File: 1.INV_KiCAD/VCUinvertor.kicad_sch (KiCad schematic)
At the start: 159 parts, among them J10 FAN2, J11 PUMP1, J12 PUMP2, J7 PowerSupply, J8 FAN1, J9 BRAKE LIGHT, K1 IM06DGR, Q1 2N7002, Q10 2N7002, Q11 2N7002, Q12 2N7002, Q13 BC848C, Q14 2N7002, Q15 IRLZ44N, Q16 IRLZ44N, Q17 IRLZ44N, Q18 2N7002, Q19 IRLZ44N, Q2 2N7002, Q3 2N7002, Q4 2N7002, Q5 2N7002, Q6 2N7002, Q7 2N7002, Q8 2N7002, Q9 2N7002, U1 TJA1448ATK, U2 REF3433T, U3 TLV76150DCY

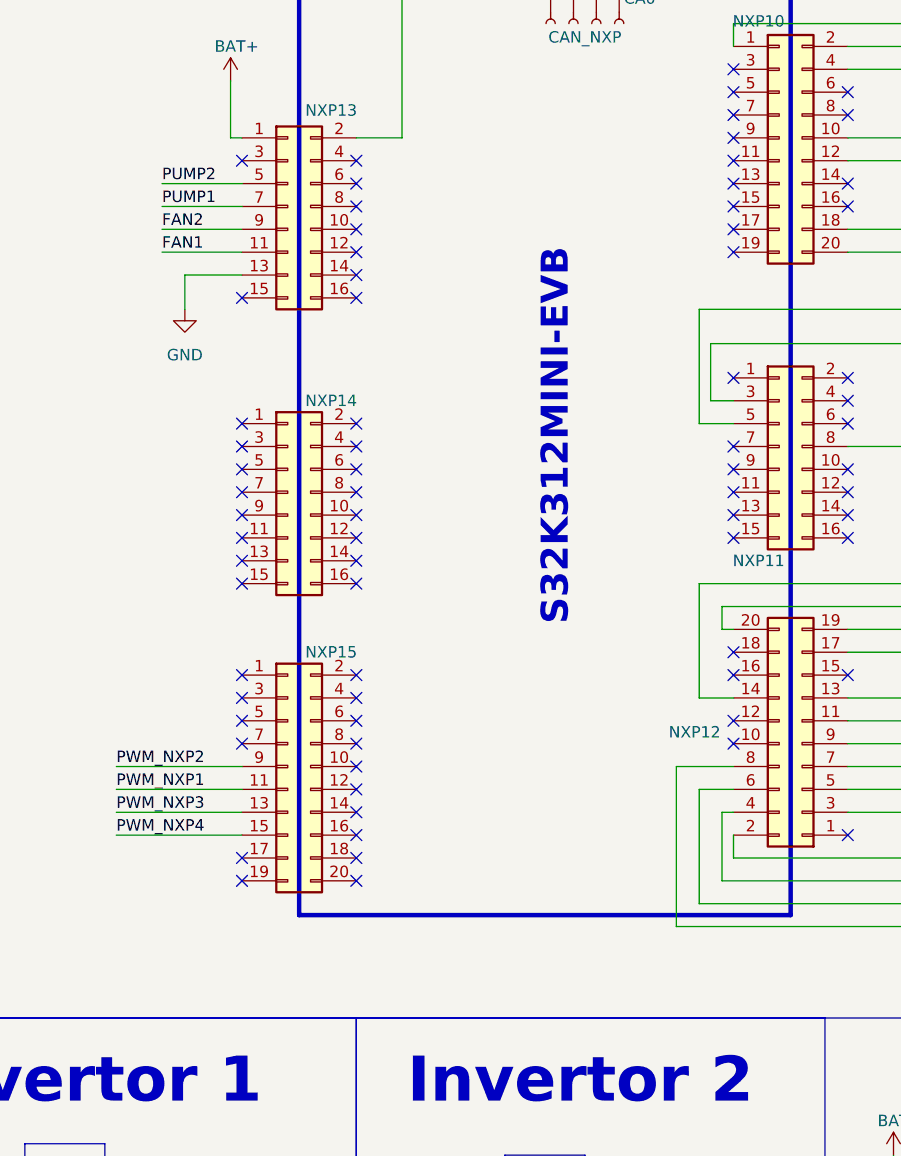
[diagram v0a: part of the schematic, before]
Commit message: FAN&PUMP pin change
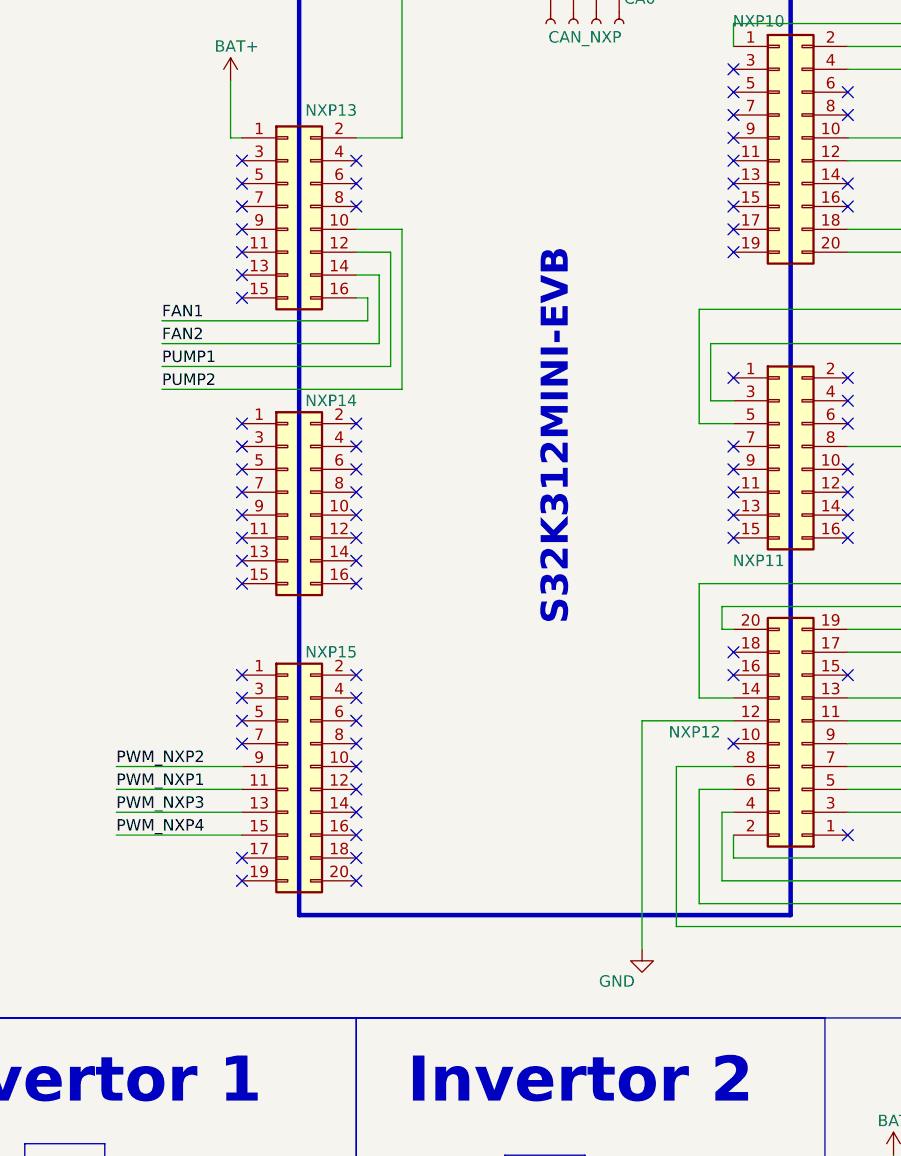
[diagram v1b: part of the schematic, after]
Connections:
- net FAN1: now also NXP13.16 (Pin_16); no longer NXP13.11 (Pin_11)
- net FAN2: now also NXP13.14 (Pin_14); no longer NXP13.9 (Pin_9)
- net GND: now also NXP12.12 (Pin_12); no longer NXP13.13 (Pin_13)
- net PUMP1: now also NXP13.12 (Pin_12); no longer NXP13.7 (Pin_7)
- net PUMP2: now also NXP13.10 (Pin_10); no longer NXP13.5 (Pin_5)

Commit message: Pin - GND assignment
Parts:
- R23: value 10k -> 47k
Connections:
- net FAN1: now also NXP13.14 (Pin_14); no longer NXP13.16 (Pin_16)
- net FAN2: now also NXP13.12 (Pin_12); no longer NXP13.14 (Pin_14)
- net GND: now also NXP13.13 (Pin_13)
- net PUMP1: now also NXP13.9 (Pin_9); no longer NXP13.12 (Pin_12)
- no-connect marks 81 -> 80
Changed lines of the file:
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@@
 	)
 	(no_connect
-		(at 54.61 63.5)
-	)
-	(no_connect
 		(at 109.22 60.96)
 	)
@@
 	)
 	(no_connect
-		(at 54.61 66.04)
-	)
-	(no_connect
 		(at 54.61 85.09)
 	)
@@
 	)
 	(no_connect
+		(at 54.61 63.5)
+	)
+	(no_connect
 		(at 121.92 90.17)
 	)
@@
 	)
 	(no_connect
-		(at 54.61 60.96)
-	)
-	(no_connect
 		(at 31.75 185.42)
 	)
@@
 	)
 	(no_connect
+		(at 67.31 68.58)
+	)
+	(no_connect
 		(at 109.22 92.71)
 	)
@@
 	(wire
 		(pts
+			(xy 40.64 66.04) (xy 54.61 66.04)
+		)
+		(stroke
+			(width 0)
+			(type default)
+		)
+	)
+	(wire
+		(pts
 			(xy 121.92 125.73) (xy 143.51 125.73)
 		)
@@
 	(wire
 		(pts
-			(xy 68.58 68.58) (xy 68.58 71.12)
-		)
-		(stroke
-			(width 0)
-			(type default)
-		)
-	)
-	(wire
-		(pts
 			(xy 138.43 251.46) (xy 138.43 254)
 		)
@@
 	(wire
 		(pts
-			(xy 67.31 66.04) (xy 69.85 66.04)
+			(xy 40.64 66.04) (xy 40.64 71.12)
 		)
 		(stroke
@@
 	(wire
 		(pts
-			(xy 16.51 166.37) (xy 27.94 166.37)
+			(xy 67.31 66.04) (xy 69.85 66.04)
 		)
 		(stroke
@@
 	(wire
 		(pts
-			(xy 67.31 60.96) (xy 72.39 60.96)
+			(xy 16.51 166.37) (xy 27.94 166.37)
 		)
 		(stroke
@@
 	(wire
 		(pts
-			(xy 67.31 68.58) (xy 68.58 68.58)
+			(xy 67.31 60.96) (xy 72.39 60.96)
 		)
 		(stroke
@@
 	(wire
 		(pts
+			(xy 45.72 60.96) (xy 54.61 60.96)
+		)
+		(stroke
+			(width 0)
+			(type default)
+		)
+	)
+	(wire
+		(pts
 			(xy 233.68 223.52) (xy 234.95 223.52)
 		)
@@
 	(wire
 		(pts
-			(xy 45.72 71.12) (xy 68.58 71.12)
-		)
-		(stroke
-			(width 0)
-			(type default)
-		)
-	)
-	(wire
-		(pts
 			(xy 138.43 270.51) (xy 143.51 270.51)
 		)
@@
 		)
 	)
-	(label "FAN1"
-		(at 45.72 71.12 0)
-		(effects
-			(font
-				(size 1.27 1.27)
-			)
-			(justify left bottom)
-		)
-	)
 	(label "12V_INV"
 		(at 218.44 147.32 0)
@@
 		)
 	)
+	(label "PUMP1"
+		(at 45.72 60.96 0)
+		(effects
+			(font
+				(size 1.27 1.27)
+			)
+			(justify left bottom)
+		)
+	)
 	(label "Brk_AN1"
 		(at 393.7 54.61 180)
@@
 		)
 	)
+	(label "FAN2"
+		(at 45.72 76.2 0)
+		(effects
+			(font
+				(size 1.27 1.27)
+			)
+			(justify left bottom)
+		)
+	)
 	(label "5V"
 		(at 349.25 134.62 0)
@@
 		)
 	)
+	(label "FAN1"
+		(at 45.72 73.66 0)
+		(effects
+			(font
+				(size 1.27 1.27)
+			)
+			(justify left bottom)
+		)
+	)
 	(label "ACC1"
 		(at 16.51 189.23 0)
@@
 		)
 	)
-	(label "PUMP1"
-		(at 45.72 76.2 0)
-		(effects
-			(font
-				(size 1.27 1.27)
-			)
-			(justify left bottom)
-		)
-	)
 	(label "FWD2"
 		(at 71.12 201.93 0)
@@
 		)
 	)
-	(label "FAN2"
-		(at 45.72 73.66 0)
-		(effects
-			(font
-				(size 1.27 1.27)
-			)
-			(justify left bottom)
-		)
-	)
 	(label "ECO2"
 		(at 246.38 175.26 180)
@@
 	)
 	(symbol
+		(lib_id "power:GND")
+		(at 40.64 71.12 0)
+		(unit 1)
+		(body_style 1)
+		(exclude_from_sim no)
+		(in_bom yes)
+		(on_board yes)
+		(in_pos_files yes)
+		(dnp no)
+		(property "Reference" "#PWR073"
+			(at 40.64 77.47 0)
+			(hide yes)
+			(show_name no)
+			(do_not_autoplace no)
+			(effects
+				(font
+					(size 1.27 1.27)
+				)
+			)
+		)
+		(property "Value" "GND"
+			(at 37.846 74.676 0)
+			(show_name no)
+			(do_not_autoplace no)
+			(effects
+				(font
+					(size 1.27 1.27)
+				)
+			)
+		)
+		(property "Footprint" ""
+			(at 40.64 71.12 0)
+			(hide yes)
+			(show_name no)
+			(do_not_autoplace no)
+			(effects
+				(font
+					(size 1.27 1.27)
+				)
+			)
+		)
+		(property "Datasheet" ""
+			(at 40.64 71.12 0)
+			(hide yes)
+			(show_name no)
+			(do_not_autoplace no)
+			(effects
+				(font
+					(size 1.27 1.27)
+				)
+			)
+		)
+		(property "Description" "Power symbol creates a global label with name \"GND\" , ground"
+			(at 40.64 71.12 0)
+			(hide yes)
+			(show_name no)
+			(do_not_autoplace no)
+			(effects
+				(font
+					(size 1.27 1.27)
+				)
+			)
+		)
+		(pin "1"
+		)
+		(instances
+			(project "VCUinvertor"
+				(path "/2b4b6758-f217-4dbc-8f9c-9ada5d4e488c"
+					(reference "#PWR073")
+					(unit 1)
+				)
+			)
+		)
+	)
+	(symbol
 		(lib_id "power:+12V")
 		(at 137.16 204.47 0)
@@
 			)
 		)
-		(property "Value" "10k"
+		(property "Value" "47k"
 			(at 346.202 235.712 90)
 			(show_name no)

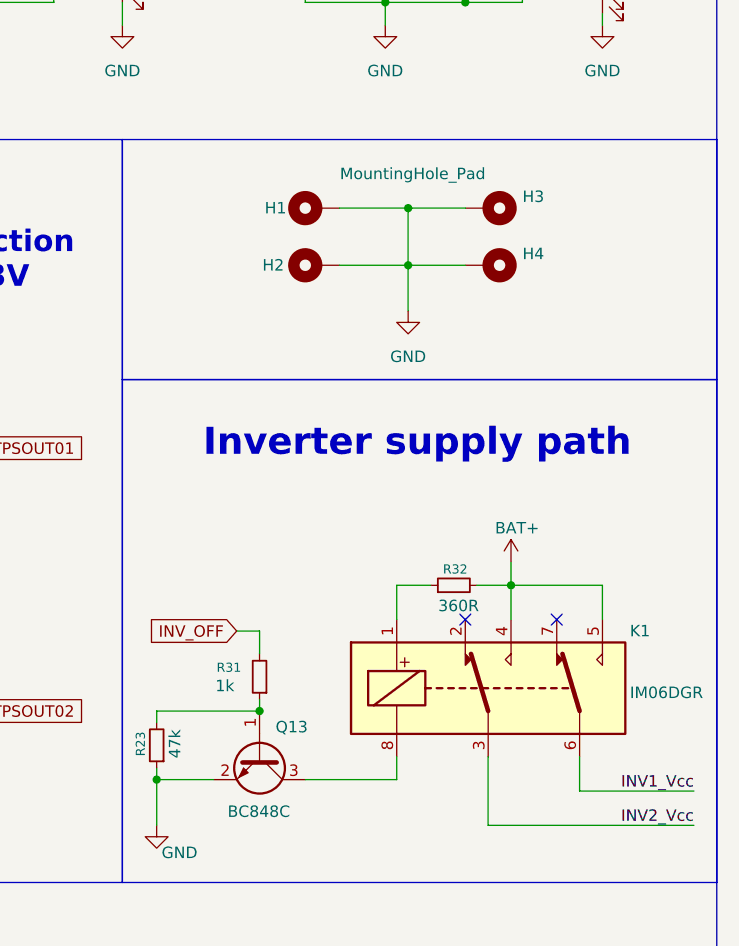
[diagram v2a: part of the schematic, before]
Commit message: Mounting Holes + Relay Flyback added
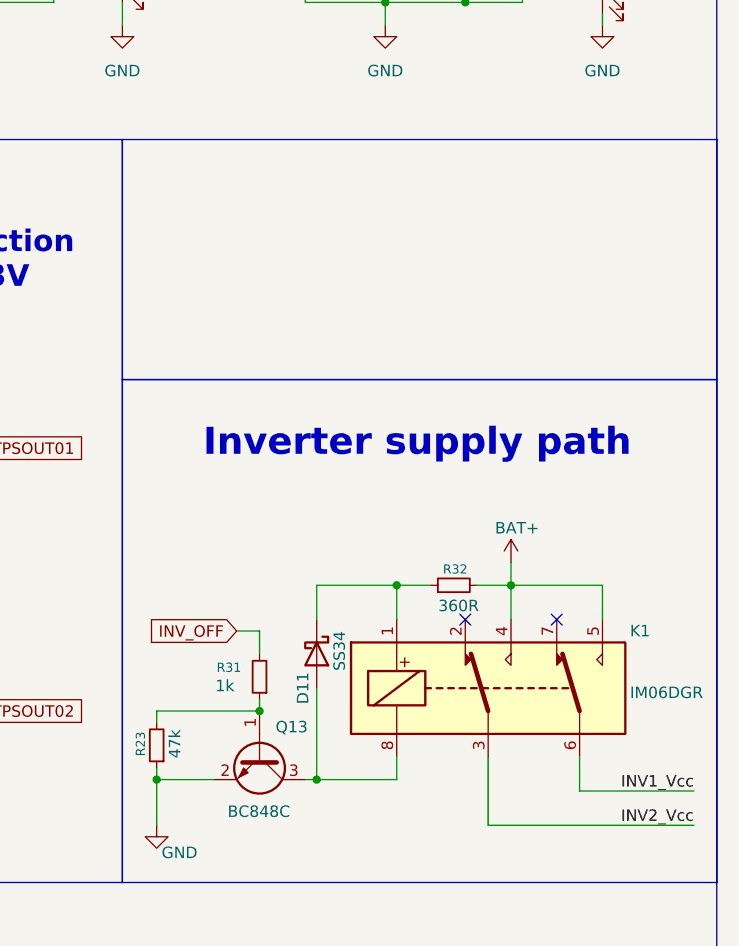
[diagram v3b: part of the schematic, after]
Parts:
- removed H1, H2, H3, H4: MountingHole_Pad, MountingHole:MountingHole_3.2mm_M3_ISO14580_Pad, symbol Mechanical:MountingHole_Pad
- added D11: SS34, Diode_SMD:D_SMA, symbol Diode:SS34
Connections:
- net at K1.8, Q13.3 (C): now also D11.2 (A)
- net at K1.1, R32.1: now also D11.1 (K)

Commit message: Connectors 2.0mm -> 2.5mm correction
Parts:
- CA1, J10, J11, J12, J8: footprint Connector_JST:JST_PH_B2B-PH-K_1x02_P2.00mm_Vertical -> Connector_JST:JST_XH_B2B-XH-A_1x02_P2.50mm_Vertical
- J9: footprint Connector_JST:JST_PH_B3B-PH-K_1x03_P2.00mm_Vertical -> Connector_JST:JST_XH_B3B-XH-A_1x03_P2.50mm_Vertical
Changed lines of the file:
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@@
 			)
 		)
-		(property "Footprint" "Connector_JST:JST_PH_B3B-PH-K_1x03_P2.00mm_Vertical"
+		(property "Footprint" "Connector_JST:JST_XH_B3B-XH-A_1x03_P2.50mm_Vertical"
 			(at 151.13 209.55 0)
 			(hide yes)
@@
 			)
 		)
-		(property "Footprint" "Connector_JST:JST_PH_B2B-PH-K_1x02_P2.00mm_Vertical"
+		(property "Footprint" "Connector_JST:JST_XH_B2B-XH-A_1x02_P2.50mm_Vertical"
 			(at 293.37 219.71 0)
 			(hide yes)
@@
 			)
 		)
-		(property "Footprint" "Connector_JST:JST_PH_B2B-PH-K_1x02_P2.00mm_Vertical"
+		(property "Footprint" "Connector_JST:JST_XH_B2B-XH-A_1x02_P2.50mm_Vertical"
 			(at 293.37 146.05 0)
 			(hide yes)
@@
 			)
 		)
-		(property "Footprint" "Connector_JST:JST_PH_B2B-PH-K_1x02_P2.00mm_Vertical"
+		(property "Footprint" "Connector_JST:JST_XH_B2B-XH-A_1x02_P2.50mm_Vertical"
 			(at 293.37 182.88 0)
 			(hide yes)
@@
 			)
 		)
-		(property "Footprint" "Connector_JST:JST_PH_B2B-PH-K_1x02_P2.00mm_Vertical"
+		(property "Footprint" "Connector_JST:JST_XH_B2B-XH-A_1x02_P2.50mm_Vertical"
 			(at 93.98 24.13 0)
 			(hide yes)
@@
 			)
 		)
-		(property "Footprint" "Connector_JST:JST_PH_B2B-PH-K_1x02_P2.00mm_Vertical"
+		(property "Footprint" "Connector_JST:JST_XH_B2B-XH-A_1x02_P2.50mm_Vertical"
 			(at 292.1 257.81 0)
 			(hide yes)

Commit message: FAN MOS correction D->S
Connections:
- net GND: now also Q15.3 (S), Q16.3 (S), Q17.3 (S), Q19.3 (S); no longer Q15.2 (D), Q16.2 (D), Q17.2 (D), Q19.2 (D)
- net at D7.2 (A), J8.2 (Pin_2): now also Q15.2 (D); no longer Q15.3 (S)
- net at D8.2 (A), J10.2 (Pin_2): now also Q16.2 (D); no longer Q16.3 (S)
- net at D9.2 (A), J11.2 (Pin_2): now also Q17.2 (D); no longer Q17.3 (S)
- net at D10.2 (A), J12.2 (Pin_2): now also Q19.2 (D); no longer Q19.3 (S)
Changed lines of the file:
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@@
 	)
 	(junction
+		(at 281.94 224.79)
+		(diameter 0)
+		(color 0 0 0 0)
+	)
+	(junction
 		(at 127 167.64)
 		(diameter 0)
@@
 	)
 	(junction
+		(at 281.94 187.96)
+		(diameter 0)
+		(color 0 0 0 0)
+	)
+	(junction
 		(at 267.97 234.95)
 		(diameter 0)
@@
 	)
 	(junction
+		(at 280.67 262.89)
+		(diameter 0)
+		(color 0 0 0 0)
+	)
+	(junction
 		(at 193.04 147.32)
 		(diameter 0)
@@
 	)
 	(junction
-		(at 345.44 134.62)
+		(at 281.94 151.13)
 		(diameter 0)
 		(color 0 0 0 0)
 	)
 	(junction
-		(at 193.04 252.73)
+		(at 345.44 134.62)
 		(diameter 0)
 		(color 0 0 0 0)
 	)
 	(junction
-		(at 280.67 262.89)
+		(at 193.04 252.73)
 		(diameter 0)
 		(color 0 0 0 0)
@@
 	)
 	(junction
-		(at 281.94 151.13)
-		(diameter 0)
-		(color 0 0 0 0)
-	)
-	(junction
 		(at 257.81 154.94)
 		(diameter 0)
@@
 	)
 	(junction
-		(at 281.94 224.79)
-		(diameter 0)
-		(color 0 0 0 0)
-	)
-	(junction
 		(at 233.68 255.27)
 		(diameter 0)
@@
 		(color 0 0 0 0)
 	)
-	(junction
-		(at 281.94 187.96)
-		(diameter 0)
-		(color 0 0 0 0)
-	)
 	(no_connect
 		(at 67.31 55.88)
@@
 	(wire
 		(pts
+			(xy 281.94 224.79) (xy 281.94 226.06)
+		)
+		(stroke
+			(width 0)
+			(type default)
+		)
+	)
+	(wire
+		(pts
 			(xy 273.05 260.35) (xy 273.05 269.24)
 		)
@@
 	(wire
 		(pts
-			(xy 281.94 189.23) (xy 281.94 187.96)
-		)
-		(stroke
-			(width 0)
-			(type default)
-		)
-	)
-	(wire
-		(pts
 			(xy 193.04 252.73) (xy 193.04 254)
 		)
@@
 	(wire
 		(pts
-			(xy 281.94 199.39) (xy 281.94 200.66)
-		)
-		(stroke
-			(width 0)
-			(type default)
-		)
-	)
-	(wire
-		(pts
 			(xy 182.88 204.47) (xy 185.42 204.47)
 		)
@@
 	(wire
 		(pts
-			(xy 281.94 162.56) (xy 281.94 163.83)
-		)
-		(stroke
-			(width 0)
-			(type default)
-		)
-	)
-	(wire
-		(pts
 			(xy 193.04 234.95) (xy 193.04 236.22)
 		)
@@
 	(wire
 		(pts
+			(xy 281.94 187.96) (xy 281.94 189.23)
+		)
+		(stroke
+			(width 0)
+			(type default)
+		)
+	)
+	(wire
+		(pts
 			(xy 360.68 139.7) (xy 360.68 140.97)
 		)
@@
 	(wire
 		(pts
-			(xy 281.94 152.4) (xy 281.94 151.13)
-		)
-		(stroke
-			(width 0)
-			(type default)
-		)
-	)
-	(wire
-		(pts
 			(xy 284.48 54.61) (xy 318.77 54.61)
 		)
@@
 	(wire
 		(pts
-			(xy 281.94 226.06) (xy 281.94 224.79)
-		)
-		(stroke
-			(width 0)
-			(type default)
-		)
-	)
-	(wire
-		(pts
 			(xy 213.36 60.96) (xy 209.55 60.96)
 		)
@@
 	(wire
 		(pts
+			(xy 281.94 236.22) (xy 281.94 237.49)
+		)
+		(stroke
+			(width 0)
+			(type default)
+		)
+	)
+	(wire
+		(pts
 			(xy 71.12 179.07) (xy 78.74 179.07)
 		)
@@
 	(wire
 		(pts
+			(xy 281.94 199.39) (xy 281.94 200.66)
+		)
+		(stroke
+			(width 0)
+			(type default)
+		)
+	)
+	(wire
+		(pts
+			(xy 281.94 151.13) (xy 281.94 152.4)
+		)
+		(stroke
+			(width 0)
+			(type default)
+		)
+	)
+	(wire
+		(pts
 			(xy 99.06 115.57) (xy 109.22 115.57)
 		)
@@
 	(wire
 		(pts
-			(xy 280.67 264.16) (xy 280.67 262.89)
-		)
-		(stroke
-			(width 0)
-			(type default)
-		)
-	)
-	(wire
-		(pts
 			(xy 340.36 130.81) (xy 340.36 134.62)
 		)
@@
 	(wire
 		(pts
-			(xy 280.67 274.32) (xy 280.67 275.59)
-		)
-		(stroke
-			(width 0)
-			(type default)
-		)
-	)
-	(wire
-		(pts
 			(xy 360.68 148.59) (xy 361.95 148.59)
 		)
@@
 	(wire
 		(pts
-			(xy 281.94 236.22) (xy 281.94 237.49)
-		)
-		(stroke
-			(width 0)
-			(type default)
-		)
-	)
-	(wire
-		(pts
 			(xy 238.76 59.69) (xy 256.54 59.69)
 		)
@@
 	(wire
 		(pts
+			(xy 280.67 262.89) (xy 280.67 264.16)
+		)
+		(stroke
+			(width 0)
+			(type default)
+		)
+	)
+	(wire
+		(pts
 			(xy 213.36 86.36) (xy 209.55 86.36)
 		)
@@
 	(wire
 		(pts
+			(xy 280.67 274.32) (xy 280.67 275.59)
+		)
+		(stroke
+			(width 0)
+			(type default)
+		)
+	)
+	(wire
+		(pts
 			(xy 127 243.84) (xy 143.51 243.84)
 		)
@@
 	(wire
 		(pts
+			(xy 281.94 162.56) (xy 281.94 163.83)
+		)
+		(stroke
+			(width 0)
+			(type default)
+		)
+	)
+	(wire
+		(pts
 			(xy 391.16 238.76) (xy 391.16 242.57)
 		)
@@
 		(lib_id "Transistor_FET:IRLZ44N")
 		(at 279.4 194.31 0)
-		(mirror x)
 		(unit 1)
 		(body_style 1)
@@
 		(dnp no)
 		(property "Reference" "Q16"
-			(at 284.226 191.516 0)
+			(at 284.226 197.104 0)
 			(show_name no)
 			(do_not_autoplace no)
@@
 		)
 		(property "Value" "IRLZ44N"
-			(at 284.226 193.548 0)
+			(at 284.226 195.072 0)
 			(show_name no)
 			(do_not_autoplace no)
@@
 		)
 		(property "Footprint" "Package_TO_SOT_THT:TO-220-3_Vertical"
-			(at 284.48 192.405 0)
+			(at 284.48 196.215 0)
 			(hide yes)
 			(show_name no)
@@
 		)
 		(property "Datasheet" "http://www.irf.com/product-info/datasheets/data/irlz44n.pdf"
-			(at 284.48 190.5 0)
+			(at 284.48 198.12 0)
 			(hide yes)
 			(show_name no)
@@
 		(lib_id "Transistor_FET:IRLZ44N")
 		(at 279.4 231.14 0)
-		(mirror x)
 		(unit 1)
 		(body_style 1)
@@
 		(dnp no)
 		(property "Reference" "Q17"
-			(at 284.226 228.346 0)
+			(at 284.226 233.934 0)
 			(show_name no)
 			(do_not_autoplace no)
@@
 		)
 		(property "Value" "IRLZ44N"
-			(at 284.226 230.378 0)
+			(at 284.226 231.902 0)
 			(show_name no)
 			(do_not_autoplace no)
@@
 		)
 		(property "Footprint" "Package_TO_SOT_THT:TO-220-3_Vertical"
-			(at 284.48 229.235 0)
+			(at 284.48 233.045 0)
 			(hide yes)
 			(show_name no)
@@
 		)
 		(property "Datasheet" "http://www.irf.com/product-info/datasheets/data/irlz44n.pdf"
-			(at 284.48 227.33 0)
+			(at 284.48 234.95 0)
 			(hide yes)
 			(show_name no)
@@
 		(lib_id "Transistor_FET:IRLZ44N")
 		(at 278.13 269.24 0)
-		(mirror x)
 		(unit 1)
 		(body_style 1)
@@
 		(dnp no)
 		(property "Reference" "Q19"
-			(at 282.956 266.446 0)
+			(at 282.956 272.034 0)
 			(show_name no)
 			(do_not_autoplace no)
@@
 		)
 		(property "Value" "IRLZ44N"
-			(at 282.956 268.478 0)
+			(at 282.956 270.002 0)
 			(show_name no)
 			(do_not_autoplace no)
@@
 		)
 		(property "Footprint" "Package_TO_SOT_THT:TO-220-3_Vertical"
-			(at 283.21 267.335 0)
+			(at 283.21 271.145 0)
 			(hide yes)
 			(show_name no)
@@
 		)
 		(property "Datasheet" "http://www.irf.com/product-info/datasheets/data/irlz44n.pdf"
-			(at 283.21 265.43 0)
+			(at 283.21 273.05 0)
 			(hide yes)
 			(show_name no)
@@
 		(lib_id "Transistor_FET:IRLZ44N")
 		(at 279.4 157.48 0)
-		(mirror x)
 		(unit 1)
 		(body_style 1)
@@
 		(dnp no)
 		(property "Reference" "Q15"
-			(at 284.226 154.686 0)
+			(at 284.226 160.274 0)
 			(show_name no)
 			(do_not_autoplace no)
@@
 		)
 		(property "Value" "IRLZ44N"
-			(at 284.226 156.718 0)
+			(at 284.226 158.242 0)
 			(show_name no)
 			(do_not_autoplace no)
@@
 		)
 		(property "Footprint" "Package_TO_SOT_THT:TO-220-3_Vertical"
-			(at 284.48 155.575 0)
+			(at 284.48 159.385 0)
 			(hide yes)
 			(show_name no)
@@
 		)
 		(property "Datasheet" "http://www.irf.com/product-info/datasheets/data/irlz44n.pdf"
-			(at 284.48 153.67 0)
+			(at 284.48 161.29 0)
 			(hide yes)
 			(show_name no)
